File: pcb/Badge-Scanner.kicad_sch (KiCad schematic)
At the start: 19 parts, among them J2 Serial, J3 NFC-Module, J4 I2C, Q3 AO3400A, U1 Pico W, U2 DS3231MZ

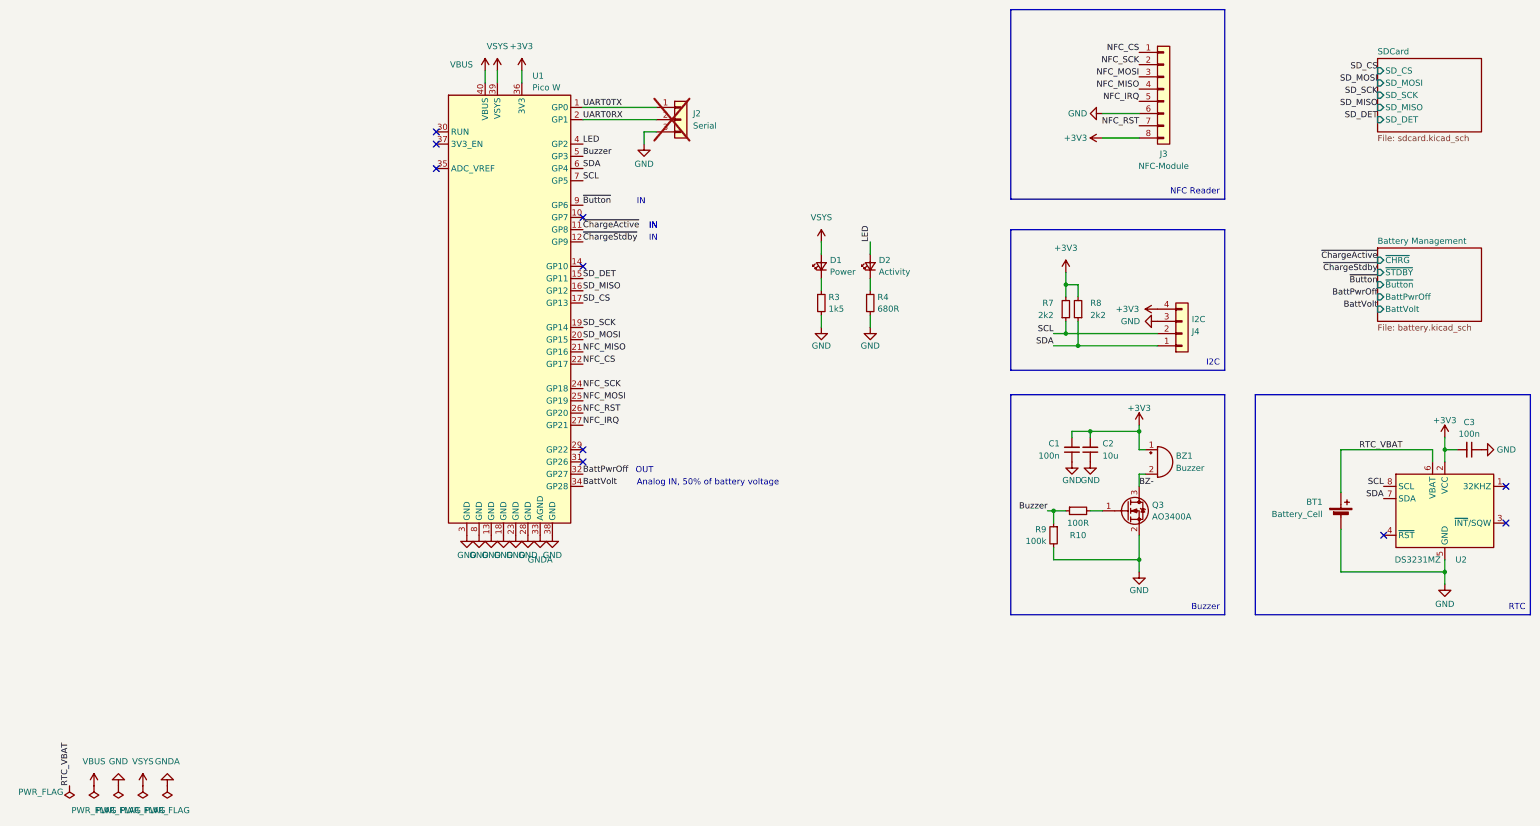
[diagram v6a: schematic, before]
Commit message: feat: optional fan connector
feat: add 3V reference for ADC
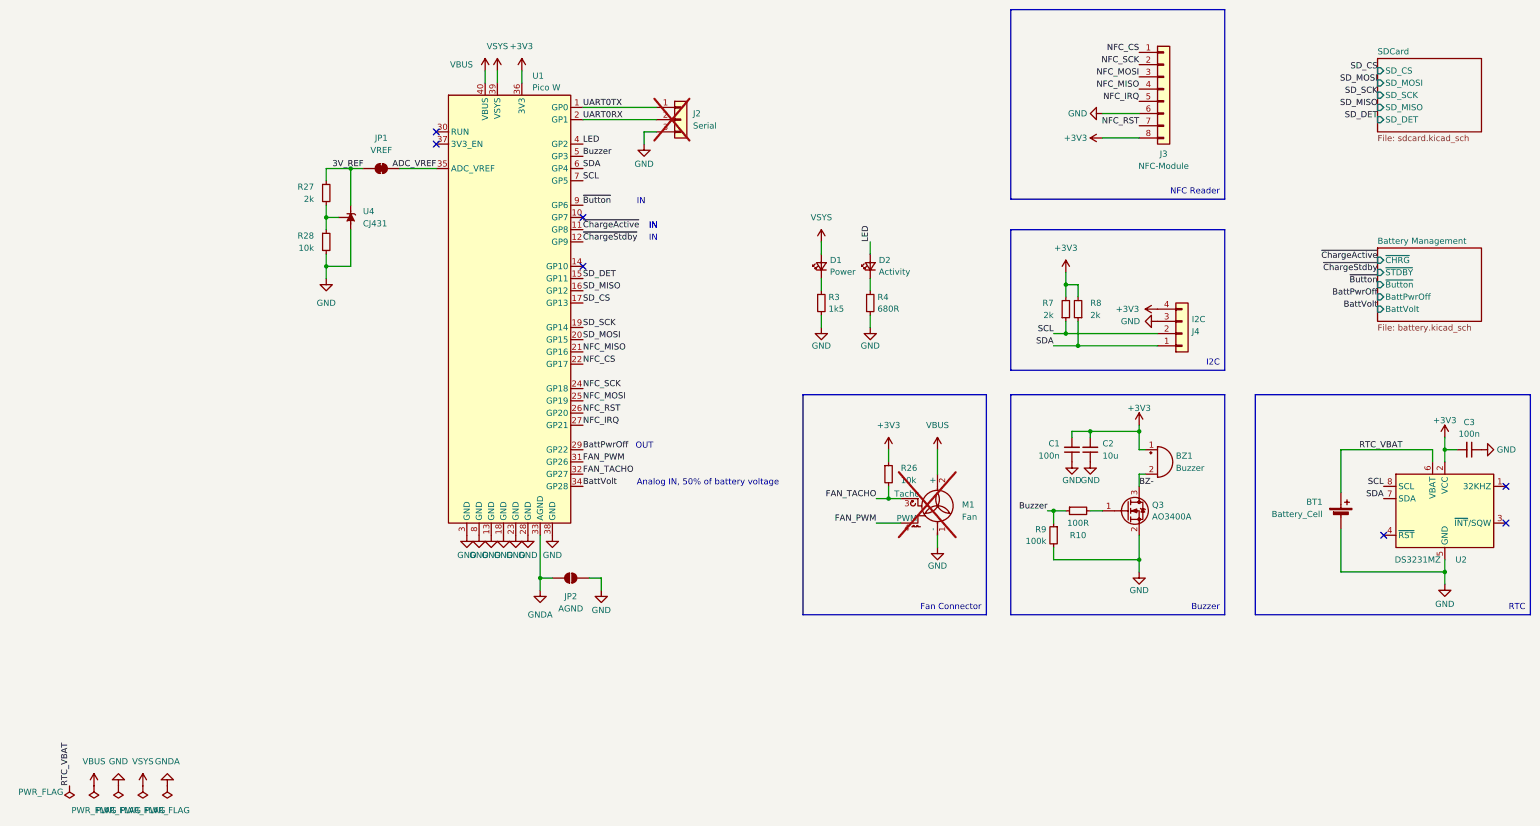
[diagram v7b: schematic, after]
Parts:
- added JP1: VREF, Jumper:SolderJumper-2_P1.3mm_Bridged_RoundedPad1.0x1.5mm, symbol Jumper:SolderJumper_2_Bridged
- added JP2: AGND, Jumper:SolderJumper-2_P1.3mm_Open_RoundedPad1.0x1.5mm, symbol Jumper:SolderJumper_2_Open
- added M1: Fan, Connector:FanPinHeader_1x04_P2.54mm_Vertical, symbol Motor:Fan_4pin
- added R26, R28: 10k, Resistor_SMD:R_0402_1005Metric, symbol Device:R_Small
- added R27: 2k, Resistor_SMD:R_0402_1005Metric, symbol Device:R_Small
- added U4: CJ431, Package_TO_SOT_SMD:SOT-23, symbol Reference_Voltage:CJ432
- R7, R8: value 2k2 -> 2k; LCSC C25900 -> C4109
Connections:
- net +3V3: now also R26.1
- net BattPwrOff: now also U1.29 (GP22); no longer U1.32 (GP27)
- net GND: now also JP2.2 (B), M1.1 (-), R28.2, U4.3 (A)
- net GNDA: now also JP2.1 (A)
- net VBUS: now also M1.2 (+)
- net FAN_PWM: now reaches U1.31 (GP26)
- net FAN_PWM: now also M1.4 (PWM)
- net ADC_VREF: now reaches U1.35 (ADC_VREF)
- net ADC_VREF: now also JP1.2 (B)
- new net: R27.2, R28.1, U4.1 (REF)
- new net 3V_REF: JP1.1 (A), R27.1, U4.2 (K)
- new net FAN_TACHO: M1.3 (Tacho), R26.2, U1.32 (GP27)
- no-connect marks 10 -> 7

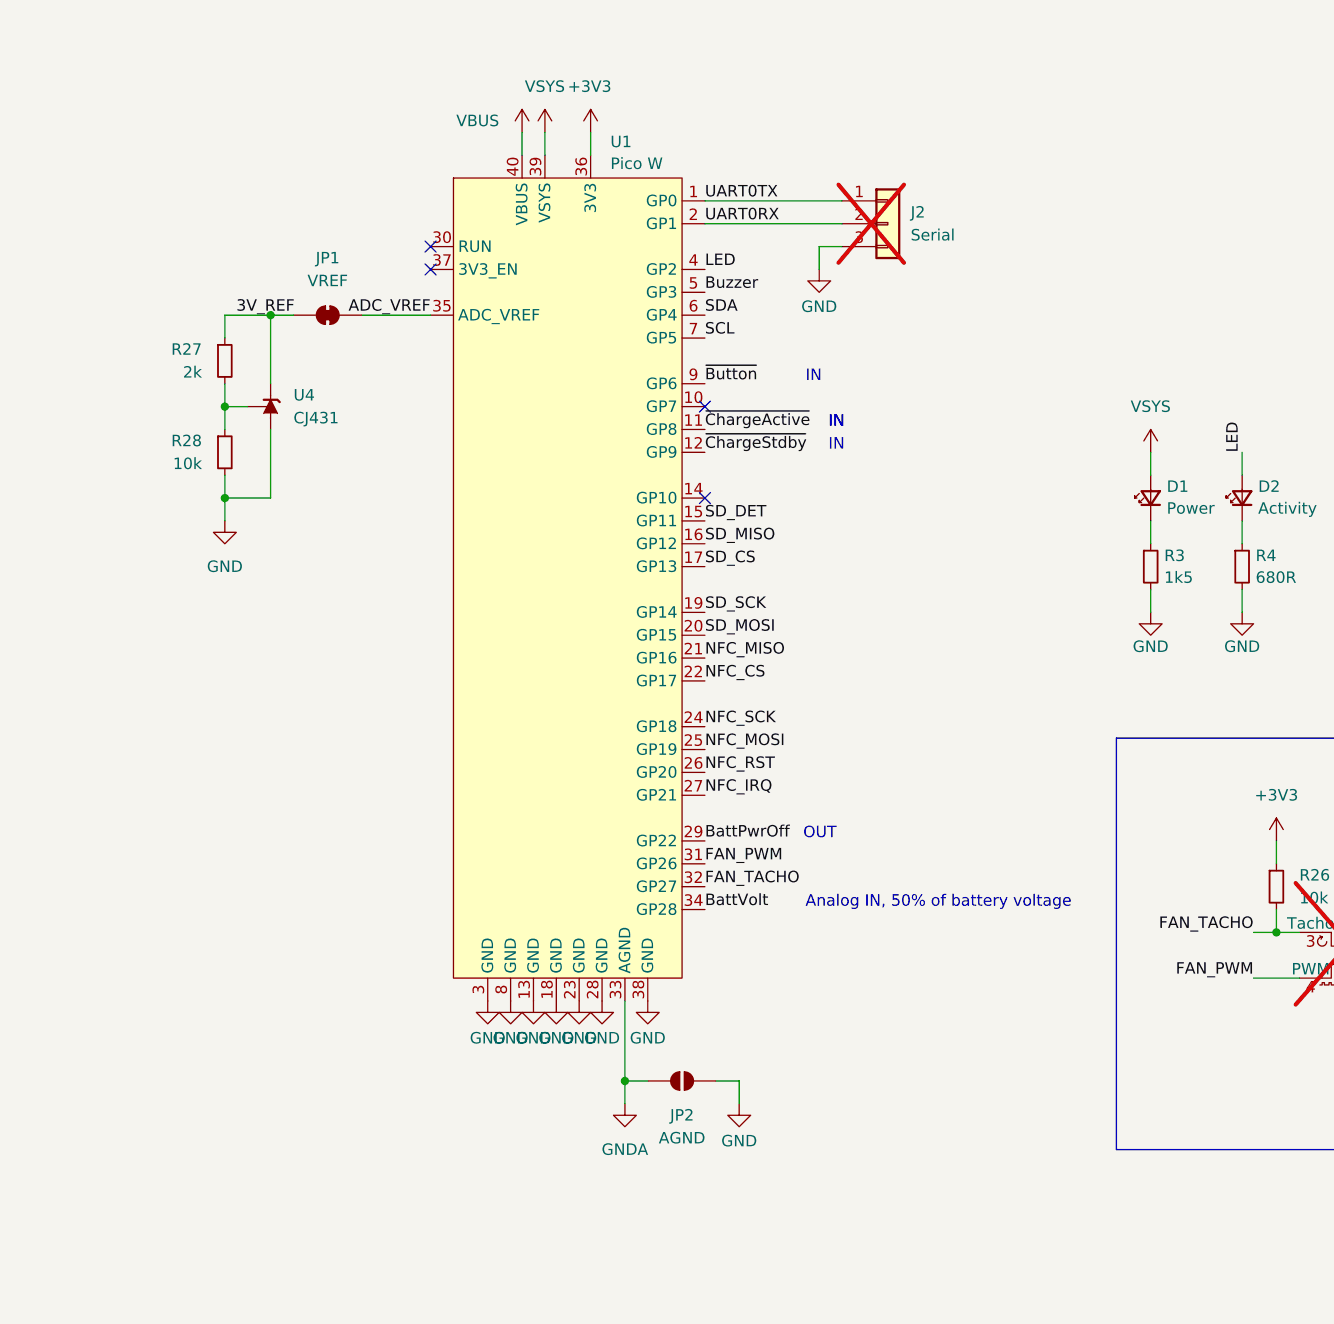
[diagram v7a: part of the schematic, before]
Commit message: fix: change resistor values for batt measurement
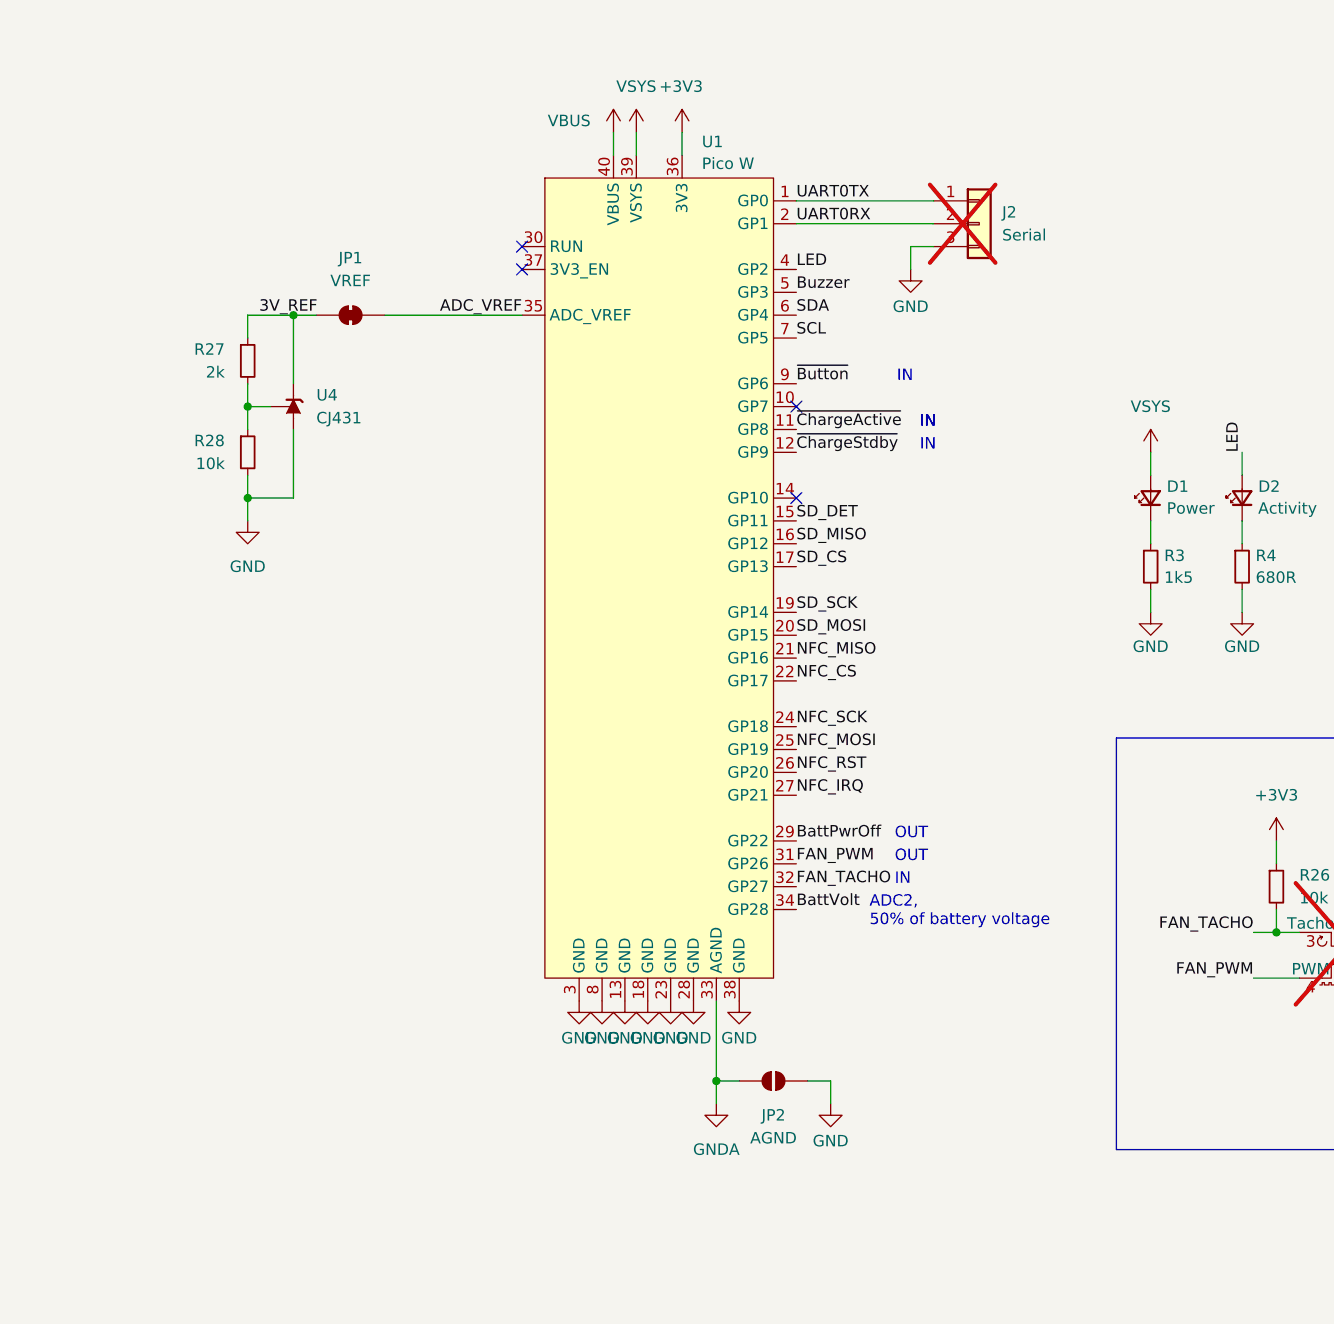
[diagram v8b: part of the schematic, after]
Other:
- note added: "ADC2, 50% of battery voltage"
- note removed: "Analog IN, 50% of battery voltage"
- moved on the sheet: J2, JP1, JP2, R27, R28, U1, U4
